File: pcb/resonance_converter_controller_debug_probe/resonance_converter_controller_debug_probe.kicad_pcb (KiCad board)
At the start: 2 copper layers, 21 x 4.8 mm, 270 parts, among them J1 USB_C_Receptacle_USB2.0_14P, J10 Micro_SD_Card_Det2, J11 Bus_M.2_Socket_E, J2 SFP, J3 USB_A, J4 USB_C_Receptacle_USB2.0_14P, J5 USB_C_Receptacle_PowerOnly_6P, J6 FX18-120S-0.8SH, J7 RJ45_JK00177, J8 Conn_01x15, J9 Micro_SD_Card_Det2, Q1 Q_PMOS_GDS, Q2 Q_NMOS_GDS, Q3 Q_NMOS_GDS, Q4 Q_NMOS_GDS, U1 TPS2121RUXR, U10 INA169, U11 INA169, U12 MCP4441-xxxx-ST, U13 THS4541IRGTT, U14 OPA333xxDBV, U15 THS4541IRGTT, U16 MCP4441-xxxx-ST, U17 STUSB4500QTR, U18 USB6B1, U19 FT230XQ, U2 TPD3S014, U20 USB6B1, U21 TPS2412D, U22 TPS2412D, U23 TPS2412D, U24 DP83869HM, U25 LP5912-1.1DRV, U26 LP5912-1.8DRV, U27 INA169, U28 OPA356xxDBV, U29 LP5912-2.5DRV, U3 TPS56637RPAR, U30 OSD32MP157C-512M-BAA, U31 TPS2553DRVR, U4 TPS73733DCQR, U5 TPS259474ARPWR, U6 LP5907MFX-3.3, U7 ADC3910D125IRSMT, U8 OPA333xxDBV, U9 INA169, Y1 Crystal_GND24

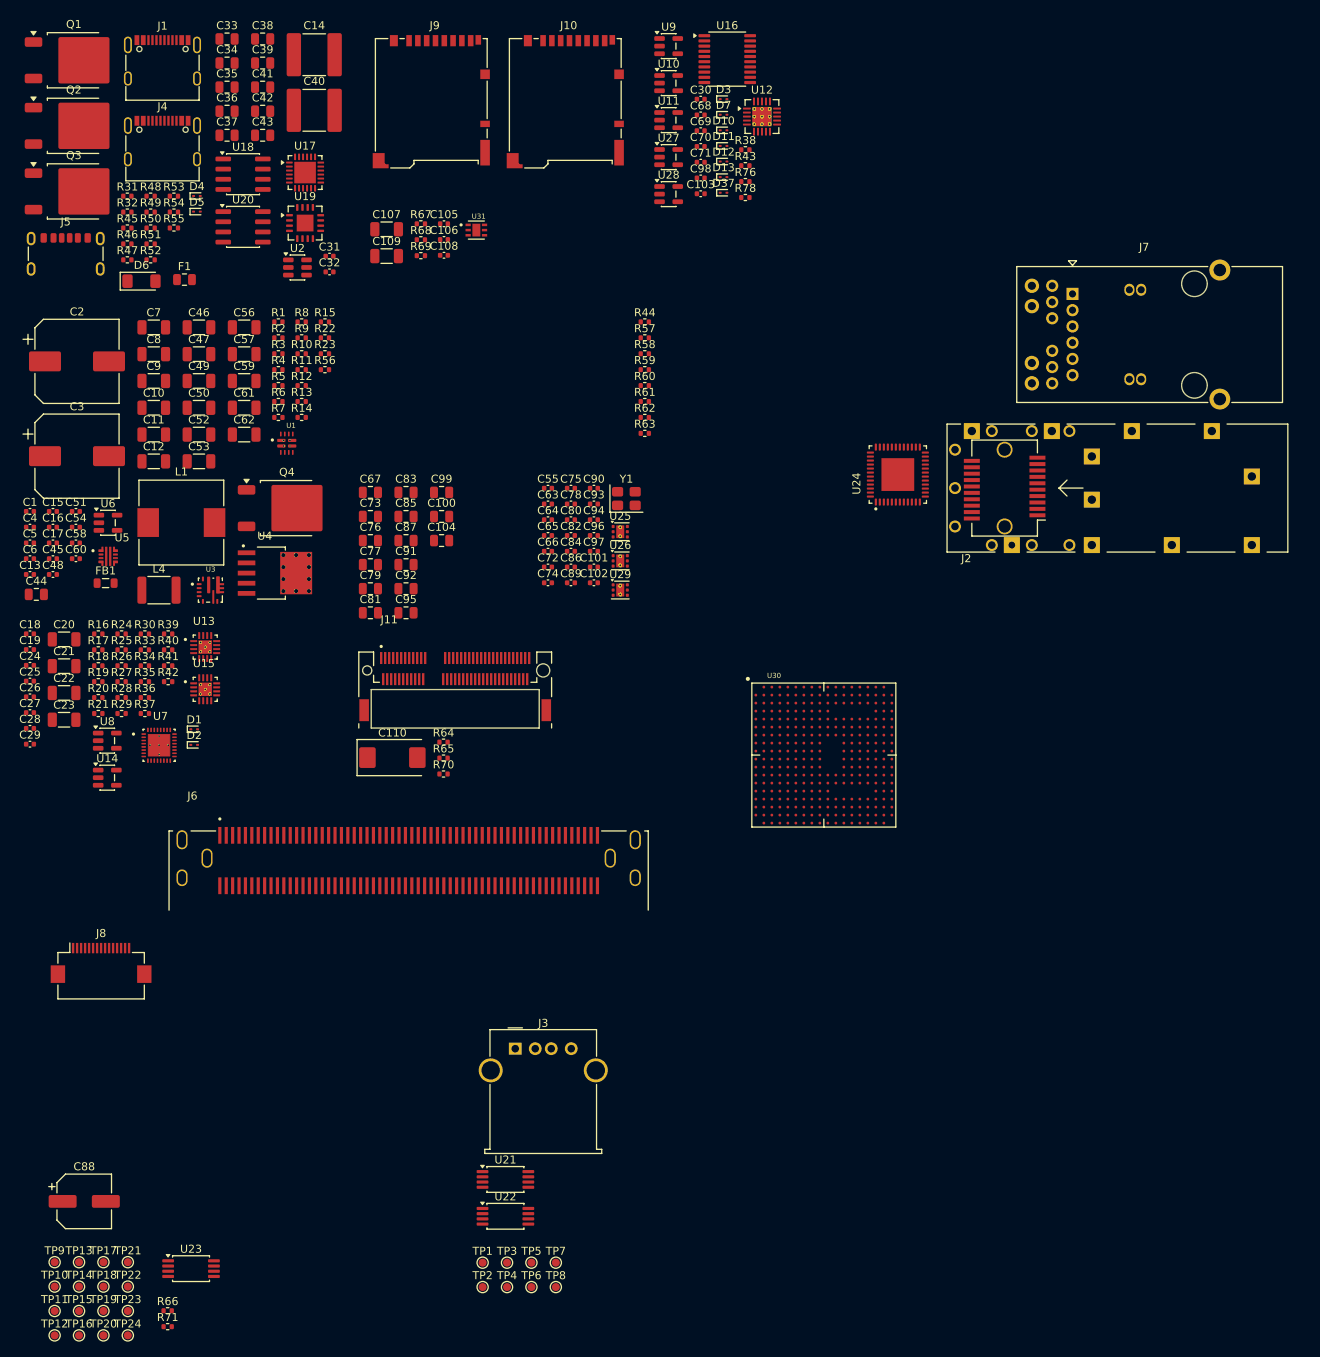
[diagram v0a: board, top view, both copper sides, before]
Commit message: Fix schematic and initial component layout
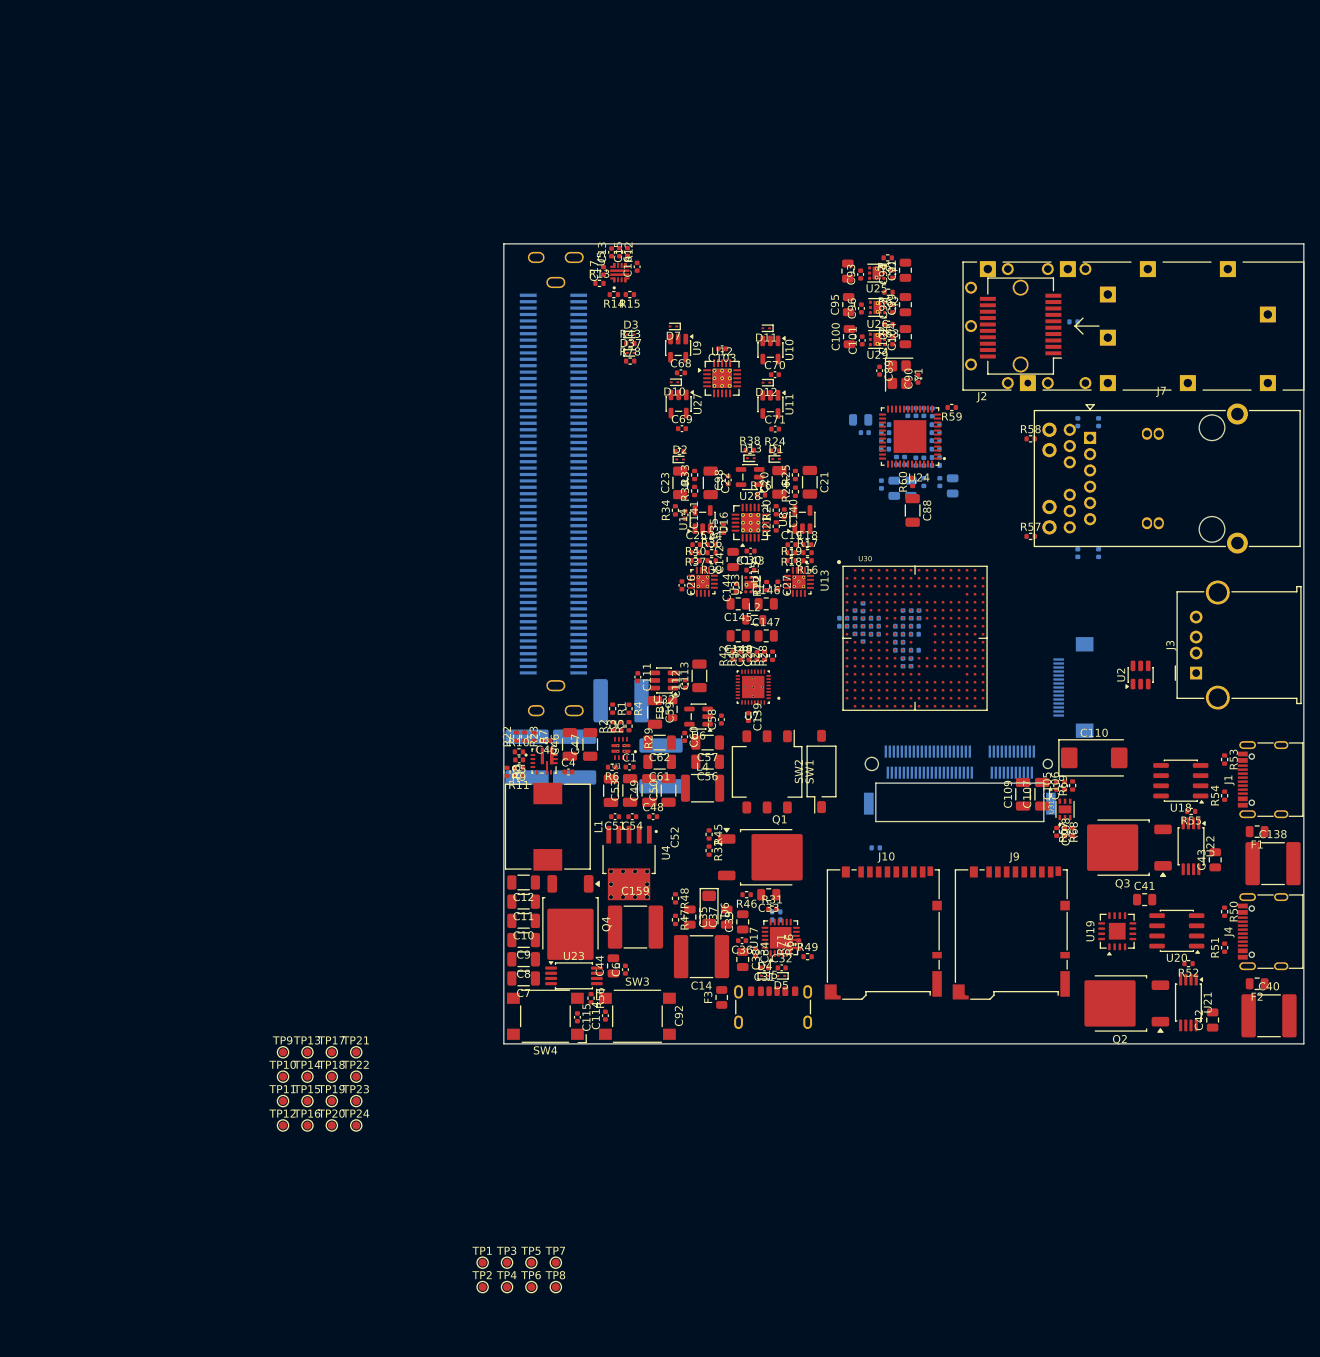
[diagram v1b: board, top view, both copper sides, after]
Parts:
- added C111: 100nF, Capacitor_SMD:C_0402_1005Metric, F.Cu at (161.2, 109.8)
- added C112: 100nF, Capacitor_SMD:C_0402_1005Metric, F.Cu at (167.2, 110.6)
- added C113: 47uF, Capacitor_SMD:C_1206_3216Metric, F.Cu at (168.9, 109.6)
- added C114: 100nF, Capacitor_SMD:C_0402_1005Metric, F.Cu at (157.2, 152.1)
- added C115: 100nF, Capacitor_SMD:C_0402_1005Metric, F.Cu at (153.7, 152.3)
- added C116: 10uF, Capacitor_SMD:C_0402_1005Metric, B.Cu at (186.9, 102.4)
- added C117: 10uF, Capacitor_SMD:C_0402_1005Metric, B.Cu at (188.4, 101.9)
- added C118: 10uF, Capacitor_SMD:C_0402_1005Metric, B.Cu at (186.9, 103.4)
- added C119: 10uF, Capacitor_SMD:C_0402_1005Metric, B.Cu at (188.4, 103.9)
- added C120: 10uF, Capacitor_SMD:C_0402_1005Metric, B.Cu at (195.4, 107.9)
- added C121: 10uF, Capacitor_SMD:C_0402_1005Metric, B.Cu at (194.4, 107.9)
- added C122: 10uF, Capacitor_SMD:C_0402_1005Metric, B.Cu at (193.9, 106.4)
- added C123: 10uF, Capacitor_SMD:C_0402_1005Metric, B.Cu at (195.9, 106.4)
- added C124: 10uF, Capacitor_SMD:C_0402_1005Metric, B.Cu at (189.4, 102.9)
- added C125: 10uF, Capacitor_SMD:C_0402_1005Metric, B.Cu at (195.9, 103.4)
- added C126: 10uF, Capacitor_SMD:C_0402_1005Metric, B.Cu at (193.9, 103.4)
- added C127: 10uF, Capacitor_SMD:C_0402_1005Metric, B.Cu at (189.4, 101.0)
- added C128: 10uF, Capacitor_SMD:C_0402_1005Metric, B.Cu at (189.4, 104.8)
- added C129: 10uF, Capacitor_SMD:C_0402_1005Metric, B.Cu at (193.9, 104.4)
- added C130: 10uF, Capacitor_SMD:C_0402_1005Metric, B.Cu at (195.9, 104.4)
- added C131: 10uF, Capacitor_SMD:C_0402_1005Metric, B.Cu at (196.4, 101.9)
- added C132: 10uF, Capacitor_SMD:C_0402_1005Metric, B.Cu at (195.4, 101.9)
- added C133: 10uF, Capacitor_SMD:C_0402_1005Metric, B.Cu at (193.9, 105.4)
- added C134: 10uF, Capacitor_SMD:C_0402_1005Metric, B.Cu at (190.9, 104.4)
- added C135: 10uF, Capacitor_SMD:C_0402_1005Metric, B.Cu at (190.9, 102.4)
- added C136: 10uF, Capacitor_SMD:C_0402_1005Metric, B.Cu at (194.4, 101.9)
- added C137: 10uF, Capacitor_SMD:C_0402_1005Metric, B.Cu at (190.9, 103.4)
- added C138: C, Capacitor_SMD:C_2220_5750Metric, F.Cu at (240.7, 133.1)
- added C139: 100nF, Capacitor_SMD:C_0402_1005Metric, F.Cu at (175.1, 114.7)
- added C140: 100nF, Capacitor_SMD:C_0402_1005Metric, F.Cu at (179.6, 89.3)
- added C141: 100nF, Capacitor_SMD:C_0402_1005Metric, F.Cu at (167.2, 89.5)
- added C142: 10u, Capacitor_SMD:C_0805_2012Metric, F.Cu at (173.2, 95.0)
- added C143: 100nF, Capacitor_SMD:C_0402_1005Metric, F.Cu at (175.3, 96.4)
- added C144: 100nF, Capacitor_SMD:C_0402_1005Metric, F.Cu at (173.6, 98.6)
- added C145: 10u, Capacitor_SMD:C_0805_2012Metric, F.Cu at (173.8, 100.6)
- added C146: 10u, Capacitor_SMD:C_0805_2012Metric, F.Cu at (177.3, 100.6)
- added C147: 10u, Capacitor_SMD:C_0805_2012Metric, F.Cu at (177.3, 104.6)
- added C148: 10u, Capacitor_SMD:C_0805_2012Metric, F.Cu at (173.8, 104.6)
- added C149: 100nF, Capacitor_SMD:C_0402_1005Metric, B.Cu at (198.5, 82.3)
- added C150: 1u, Capacitor_SMD:C_0402_1005Metric, B.Cu at (198.5, 83.3)
- added C151: 100nF, Capacitor_SMD:C_0402_1005Metric, B.Cu at (195.0, 76.6)
- added C152: 1u, Capacitor_SMD:C_0402_1005Metric, B.Cu at (196.0, 76.6)
- added C153: 100nF, Capacitor_SMD:C_0402_1005Metric, B.Cu at (194.6, 82.7)
- added C154: 1u, Capacitor_SMD:C_0402_1005Metric, B.Cu at (193.6, 82.7)
- added C155: 100nF, Capacitor_SMD:C_0402_1005Metric, B.Cu at (198.5, 80.2)
- added C156: 1u, Capacitor_SMD:C_0402_1005Metric, B.Cu at (198.5, 81.3)
- added C157: C_Polarized, Capacitor_SMD:C_2220_5750Metric, B.Cu at (153.3, 119.8)
- added C158: C_Polarized, Capacitor_SMD:C_2220_5750Metric, B.Cu at (147.4, 119.8)
- added C159: C_Polarized, Capacitor_SMD:C_2220_5750Metric, F.Cu at (160.9, 141.0)
- added F2: Fuse, Fuse:Fuse_0805_2012Metric, F.Cu at (238.7, 148.1)
- added F3: Fuse, Fuse:Fuse_0805_2012Metric, F.Cu at (171.7, 149.8)
- added L2: L, Inductor_SMD:L_0805_2012Metric, F.Cu at (175.8, 102.6)
- added R72: 10k, Resistor_SMD:R_0402_1005Metric, F.Cu at (177.3, 98.4)
- added SW1: SW_DIP_x03, Button_Switch_SMD:SW_DIP_SPSTx03_Slide_Omron_A6S-310x_W8.9mm_P2.54mm, F.Cu at (177.4, 121.6)
- added SW2: SW_DIP_x01, Button_Switch_SMD:SW_DIP_SPSTx01_Slide_Omron_A6S-110x_W8.9mm_P2.54mm, F.Cu at (184.2, 121.5)
- added SW3: SW_SPST, Button_Switch_SMD:SW_SPST_Omron_B3FS-100xP, F.Cu at (161.2, 152.2)
- added SW4: SW_SPST, Button_Switch_SMD:SW_SPST_Omron_B3FS-100xP, F.Cu at (149.7, 152.2)
- added U32: MCP1501-20xCH, Package_TO_SOT_SMD:SOT-23-6, F.Cu at (164.5, 110.2)
- added U33: LP5912-1.8DRV, Package_SON:WSON-6-1EP_2x2mm_P0.65mm_EP1x1.6mm_ThermalVias, F.Cu at (175.4, 98.2)
- C2, C3: footprint Capacitor_SMD:CP_Elec_10x10 -> Capacitor_SMD:C_2220_5750Metric; moved to B.Cu
- C34, C36: footprint Capacitor_SMD:C_0805_2012Metric -> Capacitor_SMD:C_0402_1005Metric
- C55, C63, C64, C65, C66, C72, C74, C75, C78, C80, C81, C82, C83, C84, C85, C86, C87, J11, J6, J8, R44, R64, R65, R70: moved to B.Cu
- C67, C73, C76, C77, C79: footprint Capacitor_SMD:C_0805_2012Metric -> Capacitor_SMD:C_0402_1005Metric; moved to B.Cu
- C88: footprint Capacitor_SMD:CP_Elec_6.3x3 -> Capacitor_SMD:C_1206_3216Metric
- U16: footprint Package_SO:TSSOP-20_4.4x6.5mm_P0.65mm -> Package_DFN_QFN:Texas_RGP0020H_VQFN-20-1EP_4x4mm_P0.5mm_EP2.4x2.4mm_ThermalVias
- moved Q2 170.7 mm to (221.5, 150.5), turned to 180 degrees
- moved J4 169.7 mm to (240.6, 141.6), turned to 90 degrees
- moved J1 164.7 mm to (240.6, 122.6), turned to 90 degrees
- moved C40 164.5 mm to (240.2, 152.1)
- moved C42 164.3 mm to (233.1, 152.6), turned to 90 degrees
- moved R51 160.5 mm to (234.6, 143.6), turned to 90 degrees
- moved R50 159.1 mm to (234.6, 139.1), turned to -90 degrees
- moved R52 156.8 mm to (230.1, 145.6), turned to 180 degrees
- moved Q3 154.7 mm to (221.9, 131.1), turned to 180 degrees
- moved F1 150.8 mm to (238.7, 129.1), turned to 180 degrees
- moved R54 150.2 mm to (234.6, 124.6), turned to 90 degrees
- moved C41 149.9 mm to (224.6, 137.6)
- moved C43 149.6 mm to (233.4, 132.6), turned to 90 degrees
- moved R53 149.0 mm to (234.6, 120.1), turned to -90 degrees
- moved R55 146.6 mm to (230.4, 126.5), turned to 180 degrees
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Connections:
- C105 pad 1: Net-(U31-IN) -> +3.3V
- C28 pad 1: +3.3VA -> 1V8A
- C29 pad 1: +3.3VA -> 1V8A
- J4 pad A4: Net-(Q2-S) -> Net-(F2-Pad1)
- J4 pad A9: Net-(Q2-S) -> Net-(F2-Pad1)
- J4 pad B4: Net-(Q2-S) -> Net-(F2-Pad1)
- J4 pad B9: Net-(Q2-S) -> Net-(F2-Pad1)
- J5 pad A9: Net-(D6-A) -> Net-(F3-Pad1)
- J5 pad B9: Net-(D6-A) -> Net-(F3-Pad1)
- U30 pad D3: unconnected-(U30A-PMIC_PONKEYN-PadD3) -> Net-(SW4-B)
- U30 pad G6: unconnected-(U30A-BOOT2-PadG6) -> Net-(U30A-BOOT2)
- U30 pad G7: Net-(U30A-VDD@1) -> Net-(U30A-VBAT)
- U30 pad H6: unconnected-(U30A-BOOT1-PadH6) -> Net-(U30A-BOOT1)
- U30 pad H7: Net-(U30A-VDD@1) -> Net-(U30A-VBAT)
- U30 pad J6: unconnected-(U30A-BOOT0-PadJ6) -> Net-(U30A-BOOT0)
- U30 pad J7: Net-(U30A-VDD@1) -> Net-(U30A-VBAT)
- U30 pad K3: unconnected-(U30A-VBAT-PadK3) -> Net-(U30A-VBAT)
- U30 pad K7: Net-(U30A-VDD@1) -> Net-(U30A-VBAT)
- U30 pad L7: Net-(U30A-VDD@1) -> Net-(U30A-VBAT)
- U30 pad M2: unconnected-(U30C-VREF+-PadM2) -> Net-(U30C-VREF+)
- U30 pad M3: unconnected-(U30A-NRST-PadM3) -> Net-(SW3-B)
- U30 pad M7: Net-(U30A-VDD@1) -> Net-(U30A-VBAT)
- U30 pad P4: unconnected-(U30A-EEPROM_WP-PadP4) -> Net-(U30A-EEPROM_WP)
- U31 pad 6: Net-(U31-IN) -> +3.3V
- U7 pad 12: +3.3VA -> 1V8A
- U7 pad 13: +3.3VA -> 1V8A
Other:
- board size 21 x 4.8 mm -> 100 x 100 mm
